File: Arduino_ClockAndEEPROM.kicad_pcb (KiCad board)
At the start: 2 copper layers, 0 parts

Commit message: Set design rules.
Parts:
- added BT1: Battery 3V, Connector_PinHeader_2.54mm:PinHeader_1x02_P2.54mm_Vertical, F.Cu at (160.4, 106.2)
- added C1: 22pF, Capacitor_SMD:C_0805_2012Metric_Pad1.15x1.40mm_HandSolder, F.Cu at (165.1, 108.8)
- added C2: 22pF, Capacitor_SMD:C_0805_2012Metric_Pad1.15x1.40mm_HandSolder, F.Cu at (165.3, 111.8)
- added C3: 10uF, Capacitor_SMD:C_0805_2012Metric_Pad1.15x1.40mm_HandSolder, F.Cu at (158.9, 115.6)
- added D1: LED, LED_SMD:LED_0805_2012Metric_Pad1.15x1.40mm_HandSolder, F.Cu at (160.5, 112.6)
- added J1: Serial, Connector_PinHeader_2.54mm:PinHeader_1x04_P2.54mm_Vertical, F.Cu at (99.0, 97.3)
- added J2: Digital pins, Connector_PinHeader_2.54mm:PinHeader_1x09_P2.54mm_Vertical, F.Cu at (89.7, 97.3)
- added J3: ICSP, Connector_PinSocket_2.54mm:PinSocket_2x03_P2.54mm_Vertical, F.Cu at (106.1, 97.3)
- added J4: I2C, Connector_PinSocket_2.54mm:PinSocket_1x04_P2.54mm_Vertical, F.Cu at (94.4, 97.3)
- added R1: 330, Resistor_SMD:R_0815_2038Metric_Pad1.53x4.00mm_HandSolder, F.Cu at (154.0, 115.7)
- added R2: 10K, Resistor_SMD:R_0815_2038Metric_Pad1.53x4.00mm_HandSolder, F.Cu at (149.1, 115.7)
- added U1: 24LC1025, Package_SO:SOIJ-8_5.3x5.3mm_P1.27mm, F.Cu at (152.8, 109.5)
- added U2: 24LC1025, Package_SO:SOIJ-8_5.3x5.3mm_P1.27mm, F.Cu at (152.8, 102.5)
- added U3: DS1337S+, Package_SO:SO-8_5.3x6.2mm_P1.27mm, F.Cu at (141.3, 114.6)
- added U4: ATmega328P-AU, Package_QFP:TQFP-32_7x7mm_P0.8mm, F.Cu at (141.7, 104.9)
- added Y1: Xtal 32MHz, Crystal:Crystal_SMD_MicroCrystal_CC7V-T1A-2Pin_3.2x1.5mm, F.Cu at (165.3, 105.6)
- added Y2: Xtal 16MHz, Crystal:Crystal_SMD_5032-2Pin_5.0x3.2mm_HandSoldering, F.Cu at (163.2, 101.5)
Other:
- net class Power added: clearance 0.2, trace_width 0.3, via_dia 1, via_drill 0.6

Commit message: Layout complete.
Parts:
- moved BT1 57.8 mm to (102.6, 105.5)
- moved Y2 53.8 mm to (109.8, 107.4)
- moved C2 48.5 mm to (116.8, 108.7)
- moved C1 48.3 mm to (116.8, 106.4)
- moved R2 44.1 mm to (107.0, 102.7), turned to 180 degrees
- moved J2 34.6 mm to (112.4, 123.4), turned to 90 degrees
- moved U4 30.1 mm to (113.7, 115.8)
- moved J4 30.1 mm to (124.1, 102.2), turned to 90 degrees
- moved Y1 29.9 mm to (136.8, 114.7)
- moved U2 29.1 mm to (124.7, 110.0)
- moved U1 29.0 mm to (124.8, 117.2)
- moved C3 26.6 mm to (132.3, 114.8), turned to 180 degrees
- moved D1 24.4 mm to (136.9, 118.6)
- moved R1 21.7 mm to (132.5, 118.7), turned to 180 degrees
- moved J3 16.7 mm to (105.2, 114.0)
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
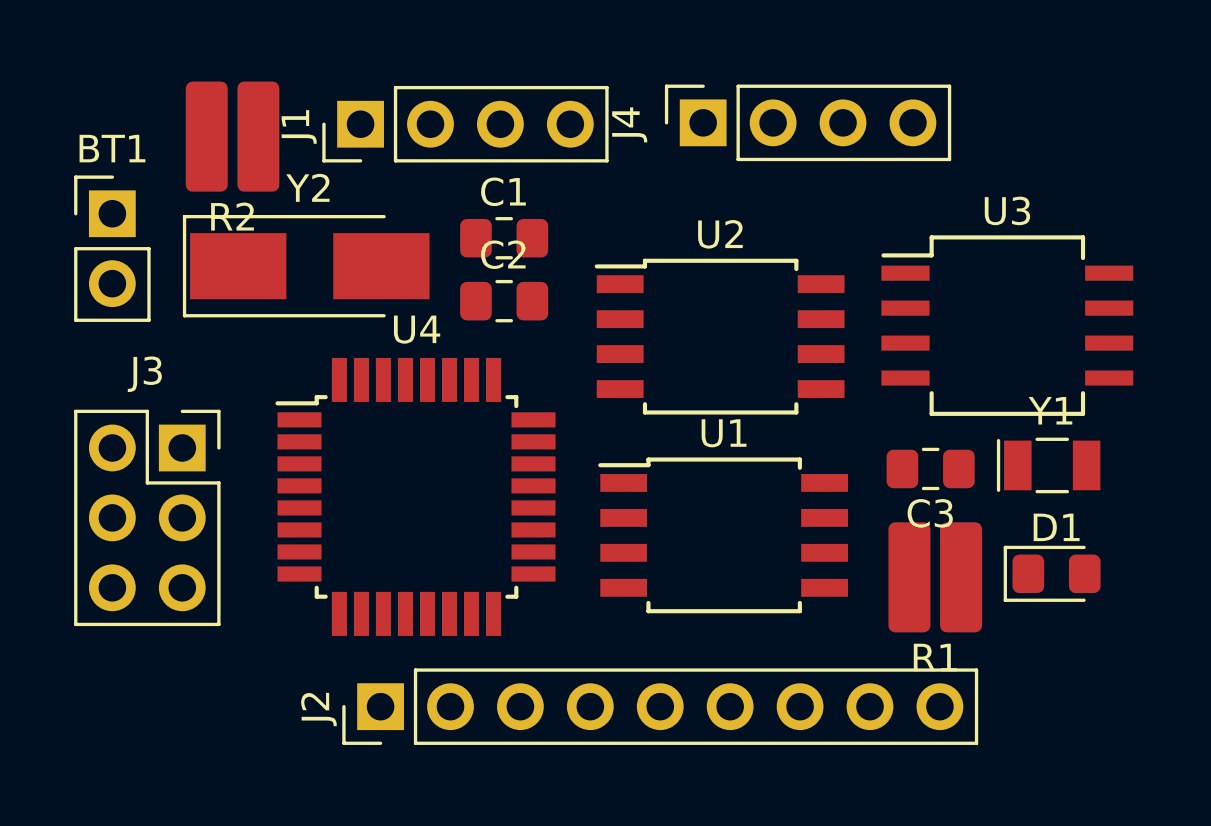
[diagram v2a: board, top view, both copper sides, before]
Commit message: Layout finalized and mounting holes are added.
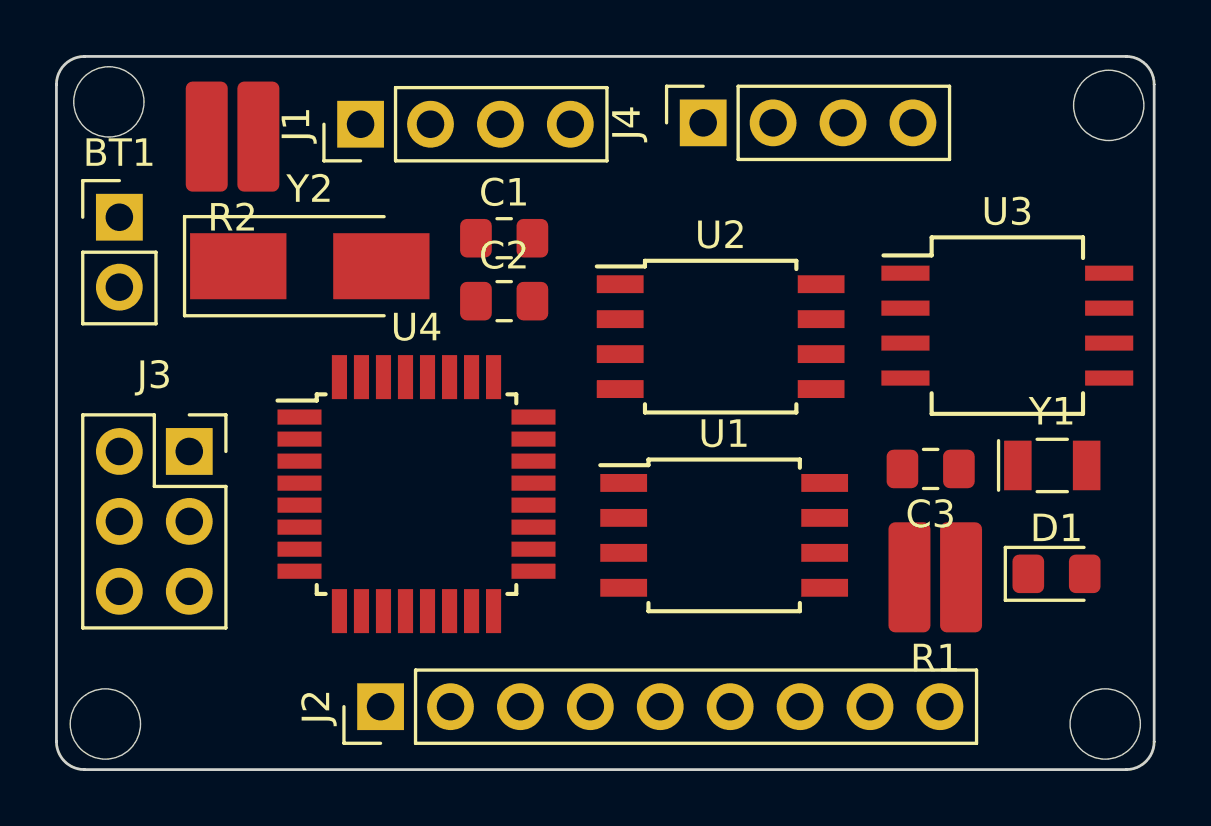
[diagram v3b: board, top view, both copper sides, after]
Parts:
- moved BT1 0.28 mm to (102.9, 105.7)
- moved J3 0.28 mm to (105.4, 114.2)
- moved U4 0.10 mm to (113.7, 115.7)
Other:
- board outline added: 39.9 x 25.9 mm
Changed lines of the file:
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@@
   (general
     (thickness 1.6)
-    (drawings 0)
+    (drawings 12)
     (tracks 0)
     (zones 0)
@@
   )
   (module Connector_PinHeader_2.54mm:PinHeader_1x02_P2.54mm_Vertical (layer F.Cu)
-    (at 102.616 105.537)
+    (at 102.87 105.664)
     (descr "Through hole straight pin header, 1x02, 2.54mm pitch, single row")
     (tags "Through hole pin header THT 1x02 2.54mm single row")
@@
   )
   (module Connector_PinSocket_2.54mm:PinSocket_2x03_P2.54mm_Vertical (layer F.Cu)
-    (at 105.156 114.046)
+    (at 105.41 114.173)
     (descr "Through hole straight socket strip, 2x03, 2.54mm pitch, double cols (from Kicad 4.0.7), script generated")
     (tags "Through hole socket strip THT 2x03 2.54mm double row")
@@
   )
   (module Package_QFP:TQFP-32_7x7mm_P0.8mm (layer F.Cu)
-    (at 113.665 115.824)
+    (at 113.665 115.723)
     (descr "32-Lead Plastic Thin Quad Flatpack (PT) - 7x7x1.0 mm Body, 2.00 mm [TQFP] (see Microchip Packaging Specification 00000049BS.pdf)")
     (tags "QFP 0.8")
@@
     )
   )
+  (gr_circle (center 138.811 101.6) (end 138.684 100.33) (layer Edge.Cuts) (width 0.05))
+  (gr_circle (center 138.684 124.072666) (end 138.557 122.802666) (layer Edge.Cuts) (width 0.05))
+  (gr_circle (center 102.362 124.072666) (end 102.235 122.802666) (layer Edge.Cuts) (width 0.05))
+  (gr_circle (center 102.489 101.473) (end 102.362 100.203) (layer Edge.Cuts) (width 0.05))
+  (gr_line (start 100.584 124.714) (end 100.584 100.838) (layer Edge.Cuts) (width 0.1))
+  (gr_line (start 139.446 125.73) (end 101.6 125.73) (layer Edge.Cuts) (width 0.1))
+  (gr_line (start 140.462 100.838) (end 140.462 124.714) (layer Edge.Cuts) (width 0.1))
+  (gr_line (start 101.6 99.822) (end 139.446 99.822) (layer Edge.Cuts) (width 0.1))
+  (gr_arc (start 139.446 100.838) (end 140.462 100.838) (angle -90) (layer Edge.Cuts) (width 0.1))
+  (gr_arc (start 139.446 124.714) (end 139.446 125.73) (angle -90) (layer Edge.Cuts) (width 0.1))
+  (gr_arc (start 101.6 124.714) (end 100.584 124.714) (angle -90) (layer Edge.Cuts) (width 0.1))
+  (gr_arc (start 101.6 100.838) (end 101.6 99.822) (angle -90) (layer Edge.Cuts) (width 0.1))
 )
